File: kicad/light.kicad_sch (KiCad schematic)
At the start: 150 parts, among them J2 USB_C_Receptacle_USB2.0_16P, J3 Barrell Jack, J4 02x04, J5 SM03B-SRSS-TB, J6 SM03B-SRSS-TB, J9 Conn_01x09_MountingPin, Q1 IRLML6344, Q2 IRLML6344, Q3 IRLML6344, SW1 Boot, SW3 On/Off, SW4 Mode, U1 RP2350A-QFN60, U10 MAX6816, U2 TPS5405DR, U3 W25Q128JVS, U4 LBEE5KL1YN-814, U5 TPS2115ADRBR, U6 TPS2120, U7 HDC1080, U8 MAX6816, U9 MAX6816, Y1 ABM8-272-T3

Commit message: more component assignment
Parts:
- R1: JLC (none) -> C142009
- R2, R3: JLC (none) -> C274341
- R4: JLC (none) -> C274872
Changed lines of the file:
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@@
 			)
 		)
+		(property "JLC" "C274341"
+			(at 90.17 57.15 90)
+			(effects
+				(font
+					(size 1.27 1.27)
+				)
+				(hide yes)
+			)
+		)
 		(pin "1"
 		)
@@
 			)
 		)
+		(property "JLC" "C142009"
+			(at 264.16 201.93 90)
+			(effects
+				(font
+					(size 1.27 1.27)
+				)
+				(hide yes)
+			)
+		)
 		(pin "2"
 		)
@@
 			)
 		)
+		(property "JLC" "C274341"
+			(at 90.17 62.23 90)
+			(effects
+				(font
+					(size 1.27 1.27)
+				)
+				(hide yes)
+			)
+		)
 		(pin "1"
 		)
@@
 			(effects
 				(font
+					(size 1.27 1.27)
+				)
+				(hide yes)
+			)
+		)
+		(property "JLC" "C274872"
+			(at 367.03 275.59 90)
+			(effects
+				(font

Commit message: mooooarr component ass ignment
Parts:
- R10, R9: JLC (none) -> C473051
- R11: JLC (none) -> C138139
- R12, R25: JLC (none) -> C25741
- R13, R15, R21: JLC (none) -> C270364
- R14: JLC (none) -> C295807
- R16: JLC (none) -> C138021
- R17: JLC (none) -> C25756
- R18, R30, R31, R32, R43: JLC (none) -> C25117
- R19, R22, R24, R27, R28, R29, R40, R41: JLC (none) -> C25744
- R20: JLC (none) -> C106225
- R23: JLC (none) -> C473534
- R26: JLC (none) -> C137933
- R36, R37: JLC (none) -> C270346
- R38, R8: JLC (none) -> C270365
- R44: JLC (none) -> C25104
- R5: JLC (none) -> C1002
- R6: JLC (none) -> C17702124
- R7: JLC (none) -> C11702
- U10, U8, U9: JLC (none) -> C41637
- U2: JLC (none) -> C488409
- U3: JLC (none) -> C97521
- U4: JLC (none) -> C6583742
- U5: JLC (none) -> C140321
- U7: JLC (none) -> C82227
- Y1: JLC (none) -> C20625731

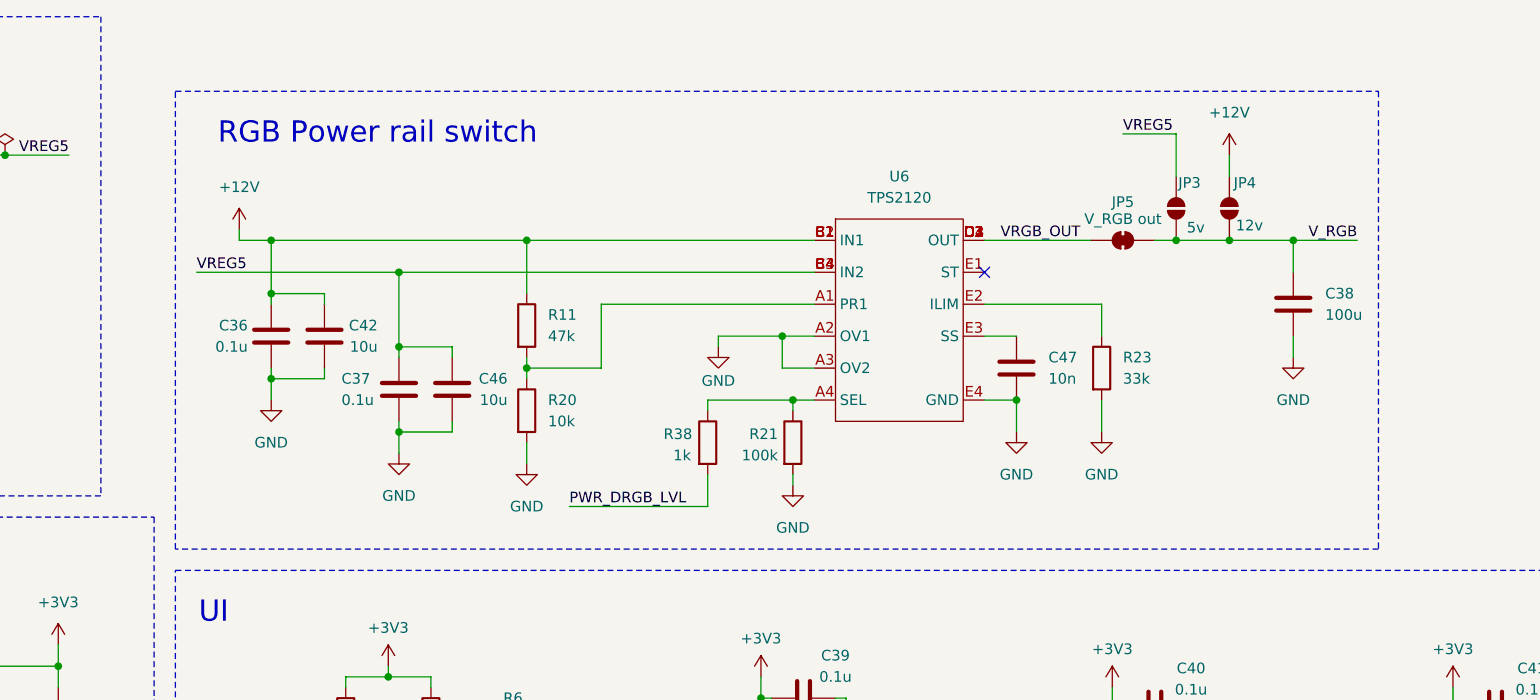
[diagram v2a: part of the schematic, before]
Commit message: replace TPS2120 with TPS2121
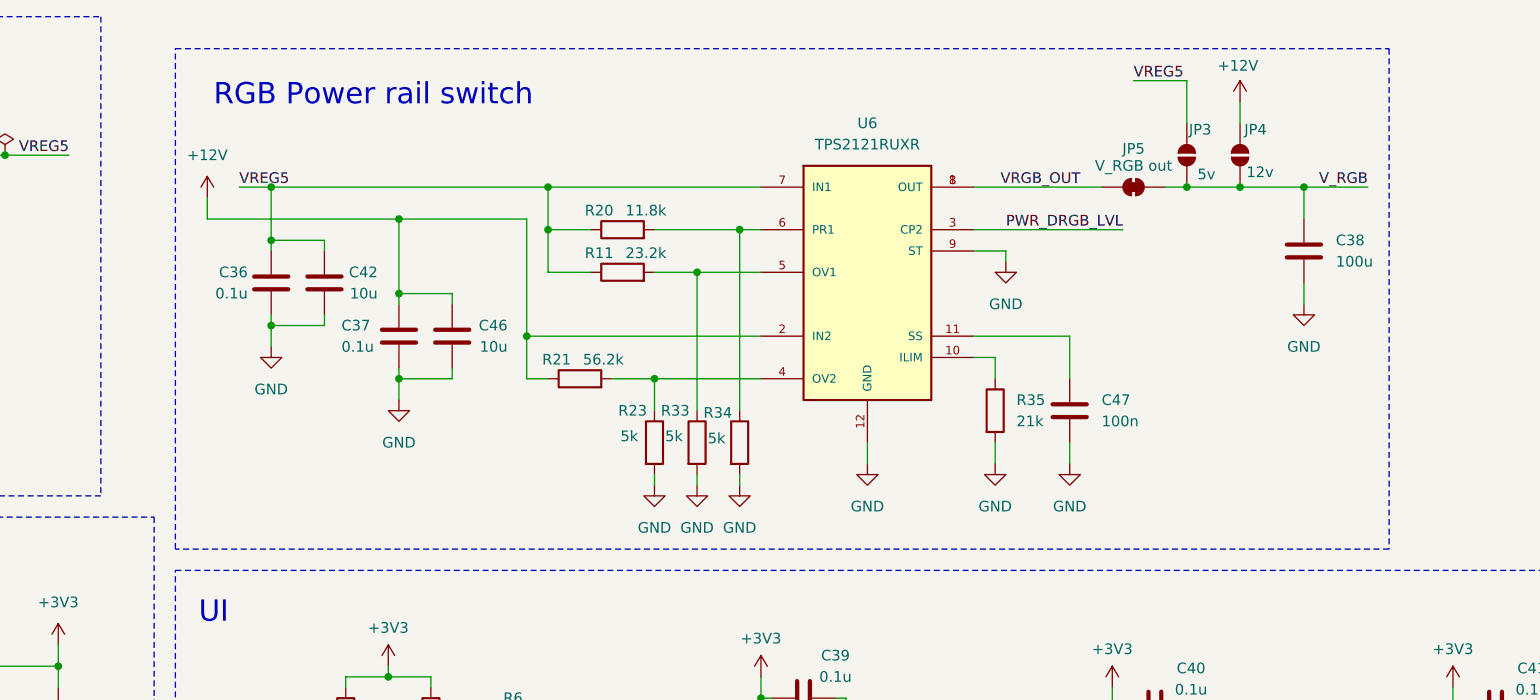
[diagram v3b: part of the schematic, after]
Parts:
- removed R38: 1k, Resistor_SMD:R_0201_0603Metric, symbol Device:R
- removed U6: TPS2120, TPS2120:TPS2120YFP, symbol TPS2120:TPS2120
- added R33, R34: 5k, Resistor_SMD:R_0201_0603Metric, symbol Device:R
- added R35: 21k, Resistor_SMD:R_0402_1005Metric, symbol Device:R
- added U6: TPS2121RUXR, TPS2121:TPS2121RUXR, symbol TPS2121RUXR:TPS2121RUXR
- C47: value 10n -> 100n; footprint Capacitor_SMD:C_0201_0603Metric -> Capacitor_SMD:C_0402_1005Metric; JLC C285010 -> C1525
- R11: value 47k -> 23.2k; JLC C138139 -> (none)
- R20: value 10k -> 11.8k; JLC C106225 -> (none)
- R21: value 100k -> 56.2k; JLC C270364 -> (none)
- R23: value 33k -> 5k; JLC C473534 -> (none)
- VR1: JLC (none) -> C250400
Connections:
- net +12V: now also C37.1, C46.1, R21.1, U6.2 (IN2); no longer C36.1, C42.1, R11.1
- net GND: now also R33.2, R34.2, R35.2, U6.12 (GND), U6.9 (ST); no longer R20.2, R21.2
- net PWR_DRGB_LVL: now also U6.3 (CP2)
- net VREG5: now also C36.1, C42.1, R11.1, R20.1, U6.7 (IN1); no longer C37.1, C46.1
- net VRGB_OUT: now also U6.1 (OUT), U6.8 (OUT)
- net at R11.2: now also R33.1, U6.5 (OV1); no longer R20.1
- net at R23.1: now also R21.2, U6.4 (OV2)
- net at C47.1: now also U6.11 (SS)
- new net: R35.1, U6.10 (ILIM)
- new net: R20.2, R34.1, U6.6 (PR1)
- no-connect marks 28 -> 27
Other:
- moved on the sheet: C36, C37, C38, C42, C46, JP3, JP4, JP5

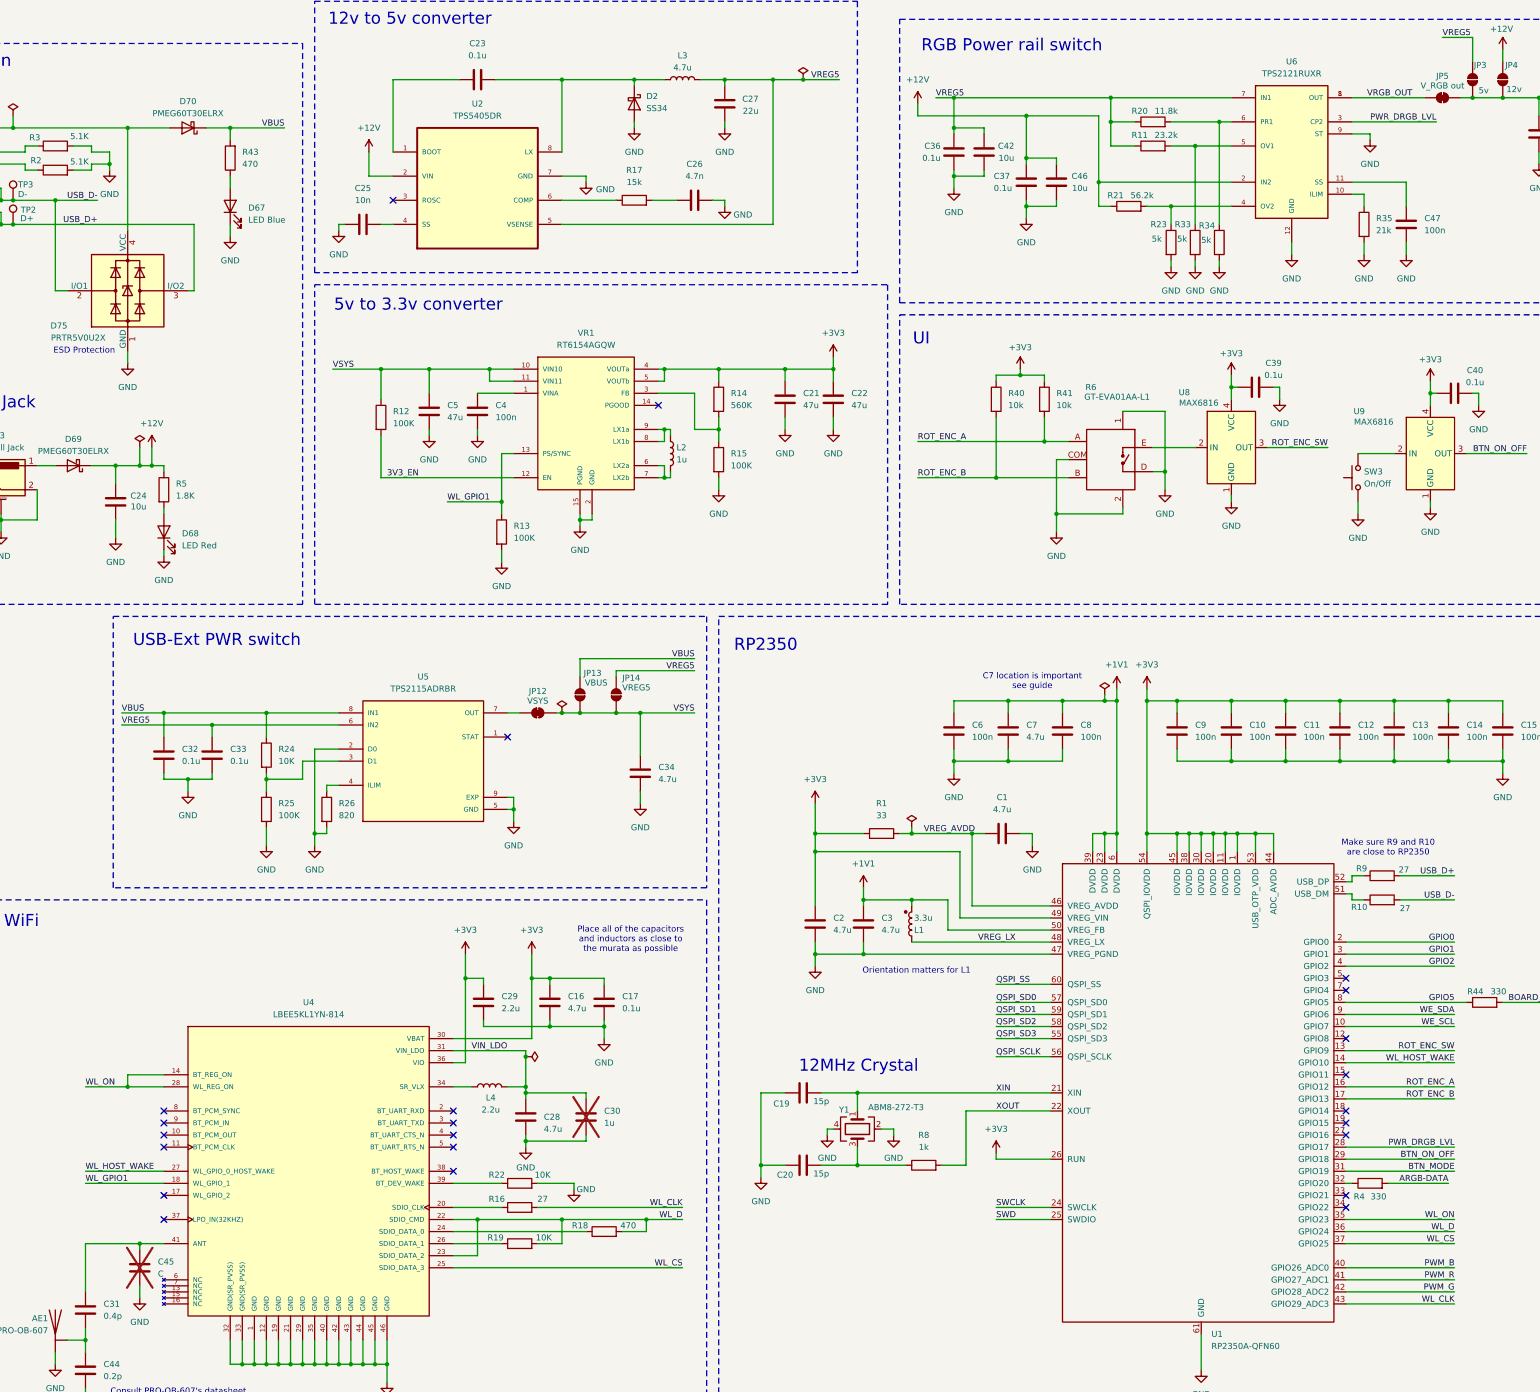
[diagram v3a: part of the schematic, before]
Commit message: component validations
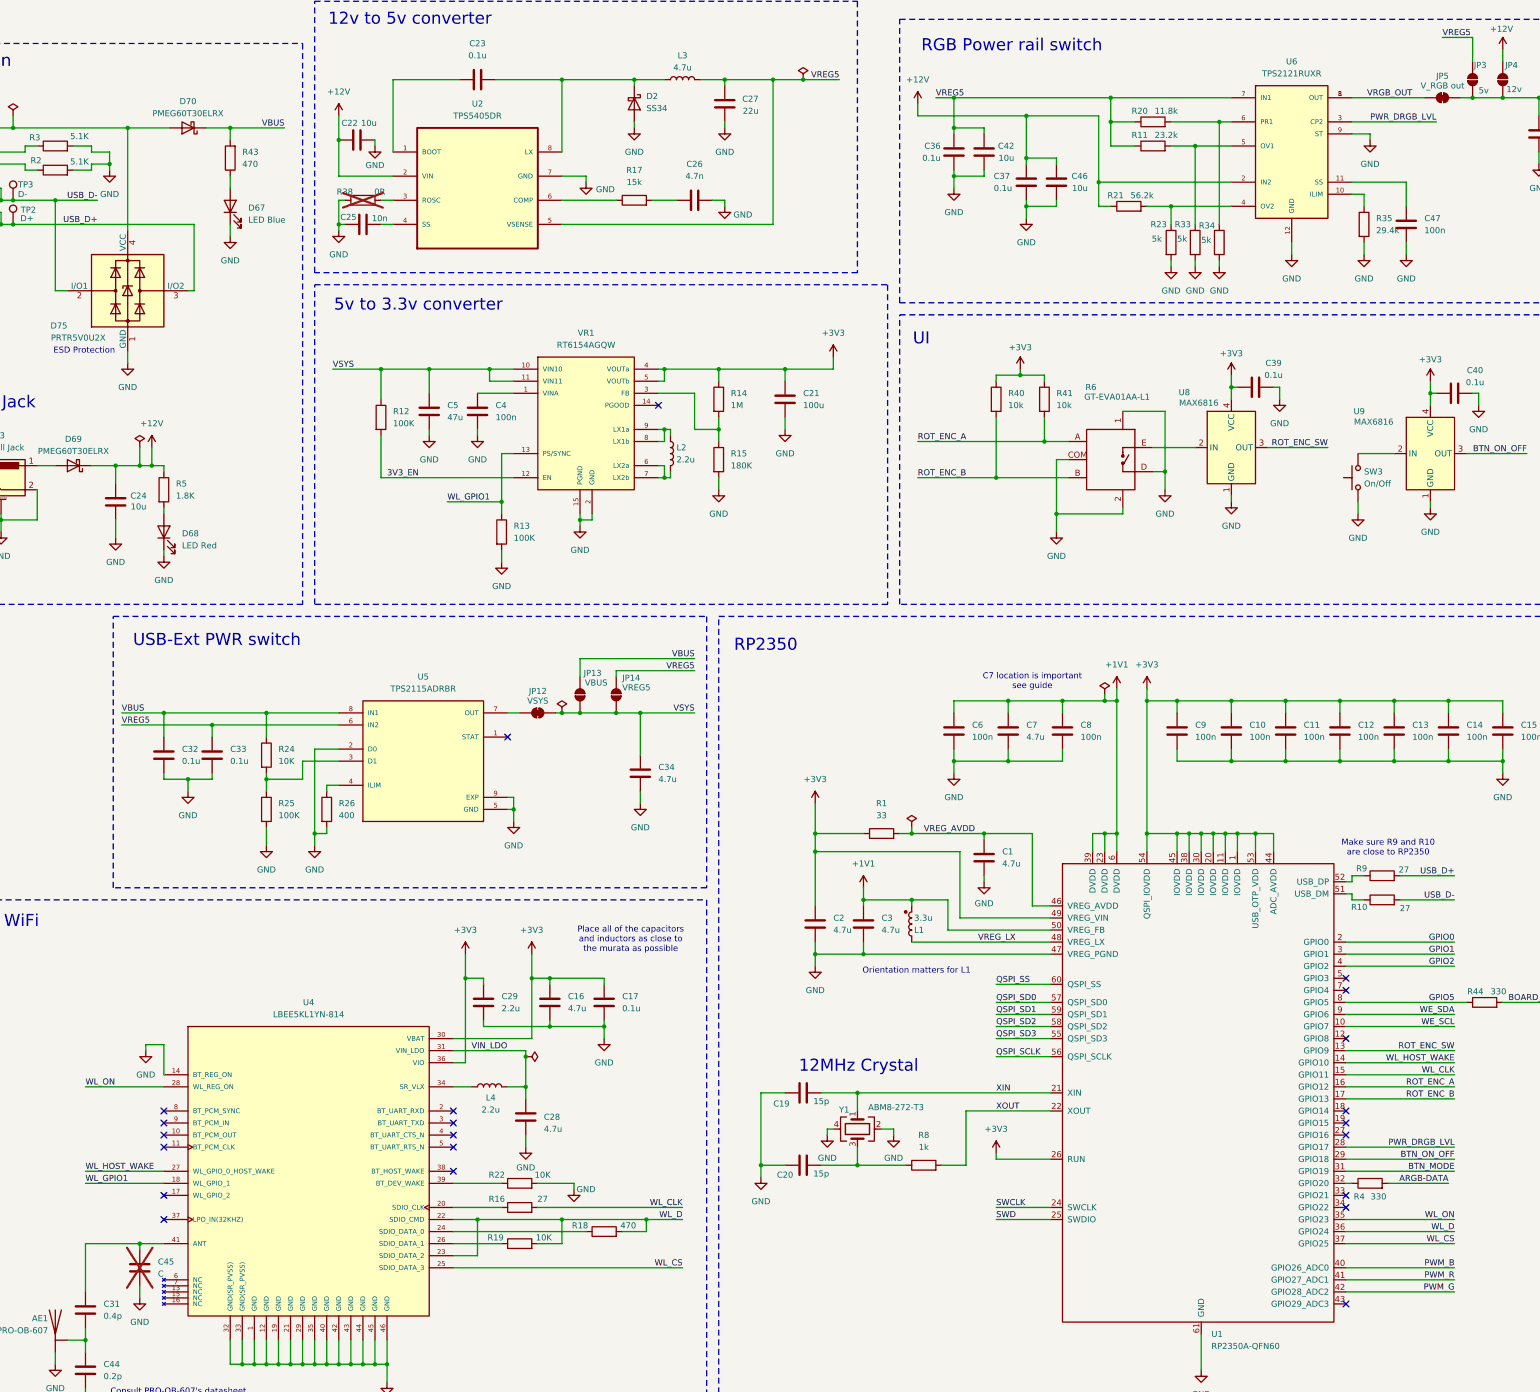
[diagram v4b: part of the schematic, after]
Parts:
- removed C30: 1u, Capacitor_SMD:C_0402_1005Metric, symbol Device:C
- added R38: 0R, Resistor_SMD:R_0603_1608Metric, symbol Device:R
- C16, C28, C29: footprint Capacitor_SMD:C_0402_1005Metric -> Capacitor_SMD:C_0201_0603Metric
- C21: value 47u -> 100u; JLC C16780 -> (none)
- C22: value 47u -> 10u; footprint Capacitor_SMD:C_0805_2012Metric -> Capacitor_SMD:C_0201_0603Metric; JLC C16780 -> (none)
- L2: value 1u -> 2.2u
- R14: value 560K -> 1M; JLC C295807 -> (none)
- R15: value 100K -> 180K; JLC C270364 -> (none)
- R26: value 820 -> 400; JLC C137933 -> (none)
- R35: value 21k -> 29.4k; JLC C25766 -> C5203996
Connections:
- net +12V: now also C22.1
- net +3V3: no longer C22.1
- net GND: now also U4.14 (BT_REG_ON), R38.1
- net WL_CLK: now also U1.15 (GPIO11); no longer U1.43 (GPIO29_ADC3)
- net WL_ON: no longer U4.14 (BT_REG_ON)
- net at U2.3 (ROSC): now also R38.2
- no-connect marks 27 -> 26
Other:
- moved on the sheet: C1

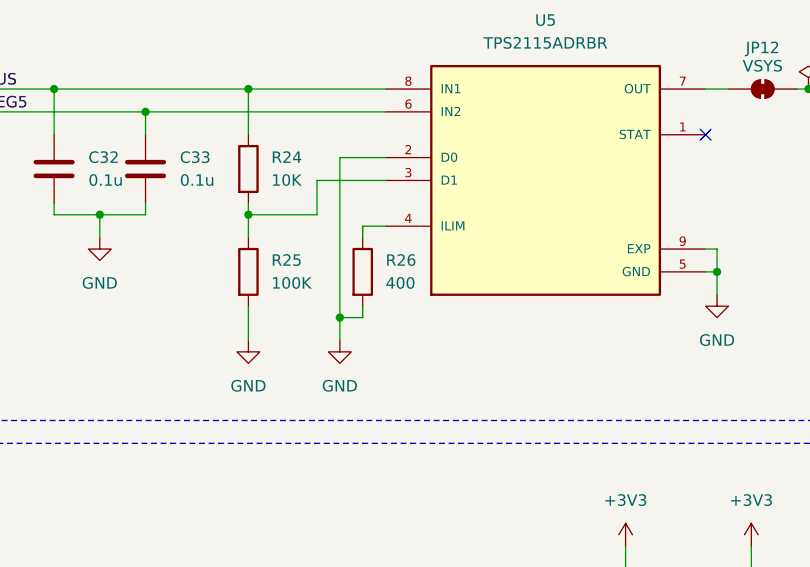
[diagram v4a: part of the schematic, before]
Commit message: style details; component assignment
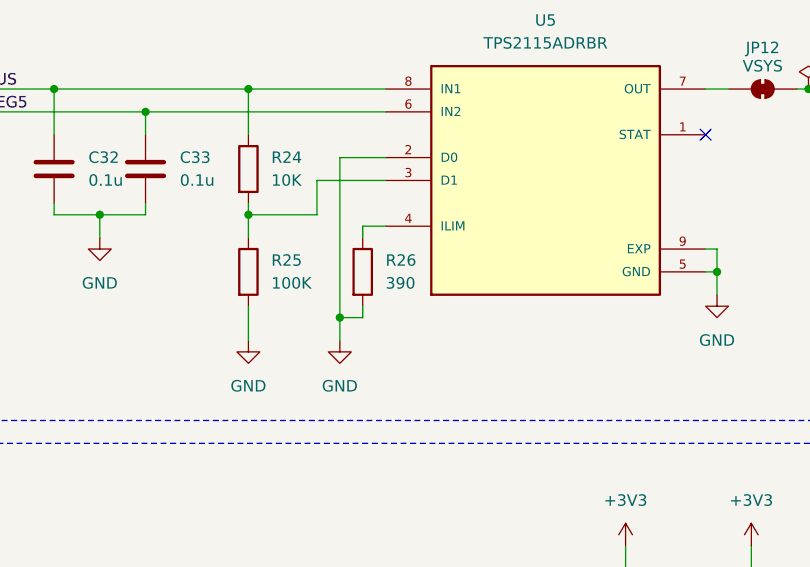
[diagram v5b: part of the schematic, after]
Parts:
- C21: JLC (none) -> C141660
- C22: JLC (none) -> C92487
- R11: JLC (none) -> C423655
- R14: JLC (none) -> C295786
- R15: JLC (none) -> C295779
- R20: JLC (none) -> C2612393
- R21: JLC (none) -> C226583
- R23, R33, R34: JLC (none) -> C1857713
- R26: value 400 -> 390; JLC (none) -> C473604
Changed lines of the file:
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@@
 			)
 		)
-		(property "JLC" ""
+		(property "JLC" "C1857713"
 			(at 325.12 77.47 0)
 			(effects
@@
 			)
 		)
-		(property "JLC" ""
+		(property "JLC" "C2612393"
 			(at 321.31 52.07 90)
 			(effects
@@
 			)
 		)
-		(property "JLC" ""
+		(property "JLC" "C1857713"
 			(at 335.28 77.47 0)
 			(effects
@@
 			)
 		)
-		(property "JLC" ""
+		(property "JLC" "C226583"
 			(at 316.23 69.85 90)
 			(effects
@@
 			)
 		)
+		(property "JLC" "C295786"
+			(at 229.87 110.49 0)
+			(effects
+				(font
+					(size 1.27 1.27)
+				)
+				(hide yes)
+			)
+		)
 		(pin "1"
 		)
@@
 			)
 		)
+		(property "JLC" "C295779"
+			(at 229.87 123.19 0)
+			(effects
+				(font
+					(size 1.27 1.27)
+				)
+				(hide yes)
+			)
+		)
 		(pin "1"
 		)
@@
 			)
 		)
+		(property "JLC" "C92487"
+			(at 153.67 55.88 90)
+			(effects
+				(font
+					(size 1.27 1.27)
+				)
+				(hide yes)
+			)
+		)
 		(pin "1"
 		)
@@
 			)
 		)
-		(property "JLC" ""
+		(property "JLC" "C1857713"
 			(at 330.2 77.47 0)
 			(effects
@@
 			)
 		)
-		(property "Value" "400"
+		(property "Value" "390"
 			(at 149.86 198.1199 0)
 			(effects
@@
 			)
 		)
-		(property "JLC" ""
+		(property "JLC" "C473604"
 			(at 147.32 196.85 0)
 			(effects
@@
 			)
 		)
-		(property "JLC" ""
+		(property "JLC" "C423655"
 			(at 321.31 57.15 90)
 			(effects
@@
 			(at 243.84 110.49 0)
 			(effects
+				(font
+					(size 1.27 1.27)
+				)
+				(hide yes)
+			)
+		)
+		(property "JLC" "C141660"
+			(at 243.84 110.49 0)
+			(effects
